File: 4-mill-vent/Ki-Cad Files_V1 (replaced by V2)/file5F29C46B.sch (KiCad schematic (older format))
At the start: 3 parts

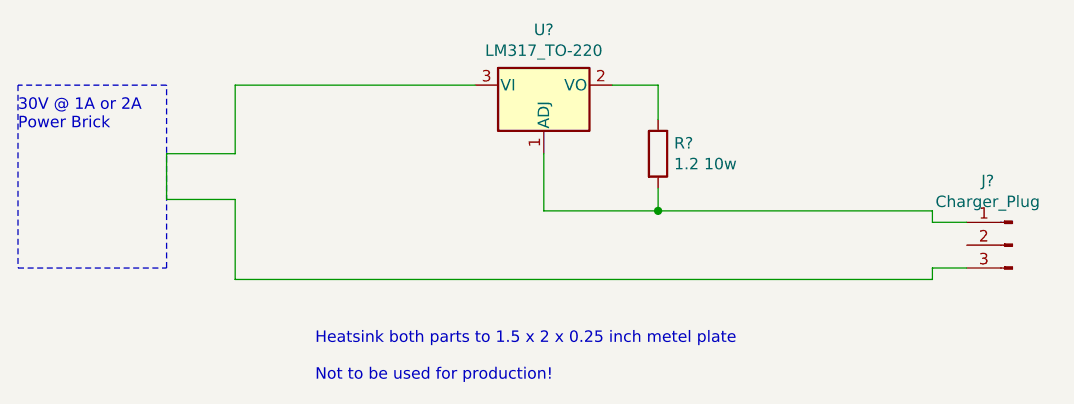
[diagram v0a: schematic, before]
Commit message: Last Update USE V2
Board test complete, all slikscreen error are fixed in v2, Full use of opamp for battery monitoring.
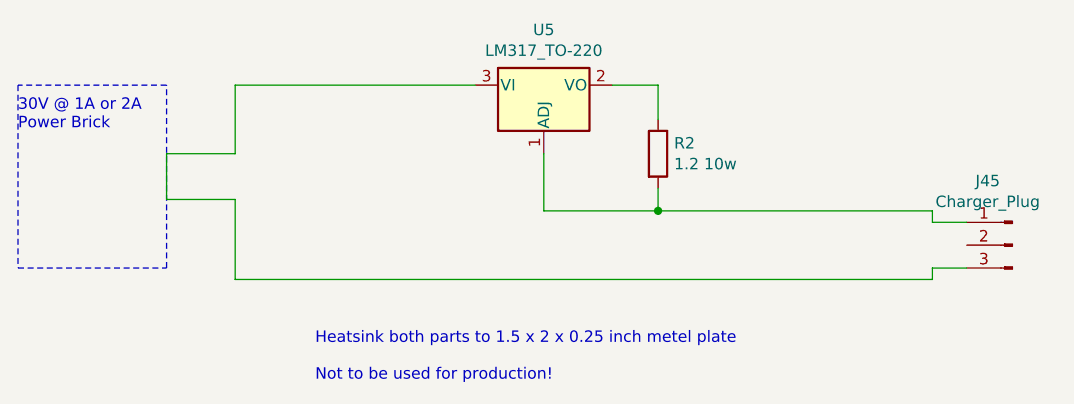
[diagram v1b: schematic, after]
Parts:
- gave numbers to parts that had none: 3
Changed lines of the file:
@@
 $EndDescr
 $Comp
-L Regulator_Linear:LM317_TO-220 U?
+L Regulator_Linear:LM317_TO-220 U5
 U 1 1 5F29C9F9
 P 5450 2800
-F 0 "U?" H 5450 3042 50  0000 C CNN
+F 0 "U5" H 5450 3042 50  0000 C CNN
 F 1 "LM317_TO-220" H 5450 2951 50  0000 C CNN
 F 2 "Package_TO_SOT_THT:TO-220-3_Vertical" H 5450 3050 50  0001 C CIN
@@
 $EndComp
 $Comp
-L Device:R R?
+L Device:R R2
 U 1 1 5F29D1A4
 P 5950 3100
-F 0 "R?" H 6020 3146 50  0000 L CNN
+F 0 "R2" H 6020 3146 50  0000 L CNN
 F 1 "1.2 10w" H 6020 3055 50  0000 L CNN
 F 2 "" V 5880 3100 50  0001 C CNN
@@
 	4100 3300 4100 3650
 $Comp
-L Connector:Conn_01x03_Male J?
+L Connector:Conn_01x03_Male J45
 U 1 1 5F2A1A8B
 P 7500 3500
-F 0 "J?" H 7608 3781 50  0000 C CNN
+F 0 "J45" H 7608 3781 50  0000 C CNN
 F 1 "Charger_Plug" H 7608 3690 50  0000 C CNN
 F 2 "" H 7500 3500 50  0001 C CNN
